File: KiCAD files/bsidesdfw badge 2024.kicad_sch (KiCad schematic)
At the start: 28 parts, among them Q1 BC548, U1 NE555P, U2 74HC595

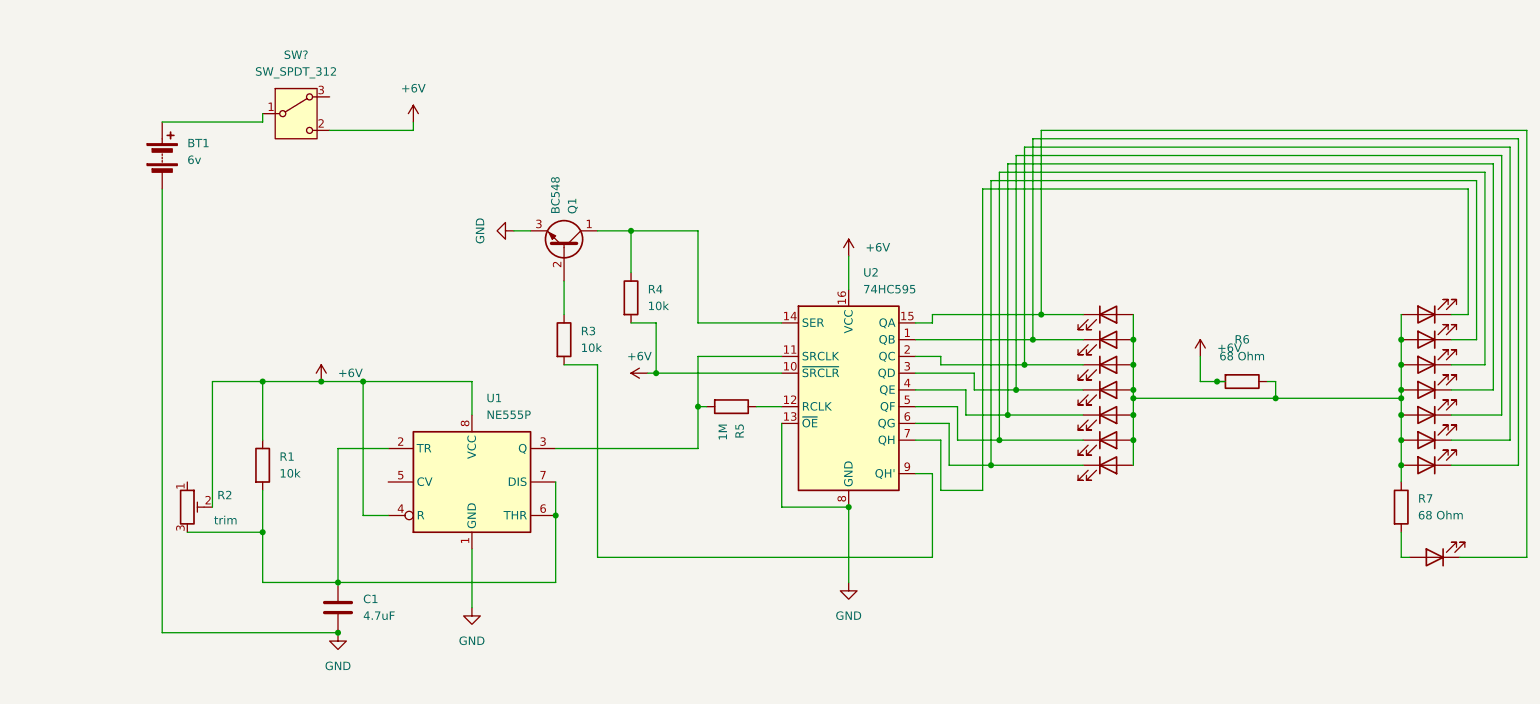
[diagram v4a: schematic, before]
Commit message: adjust the 555 drive
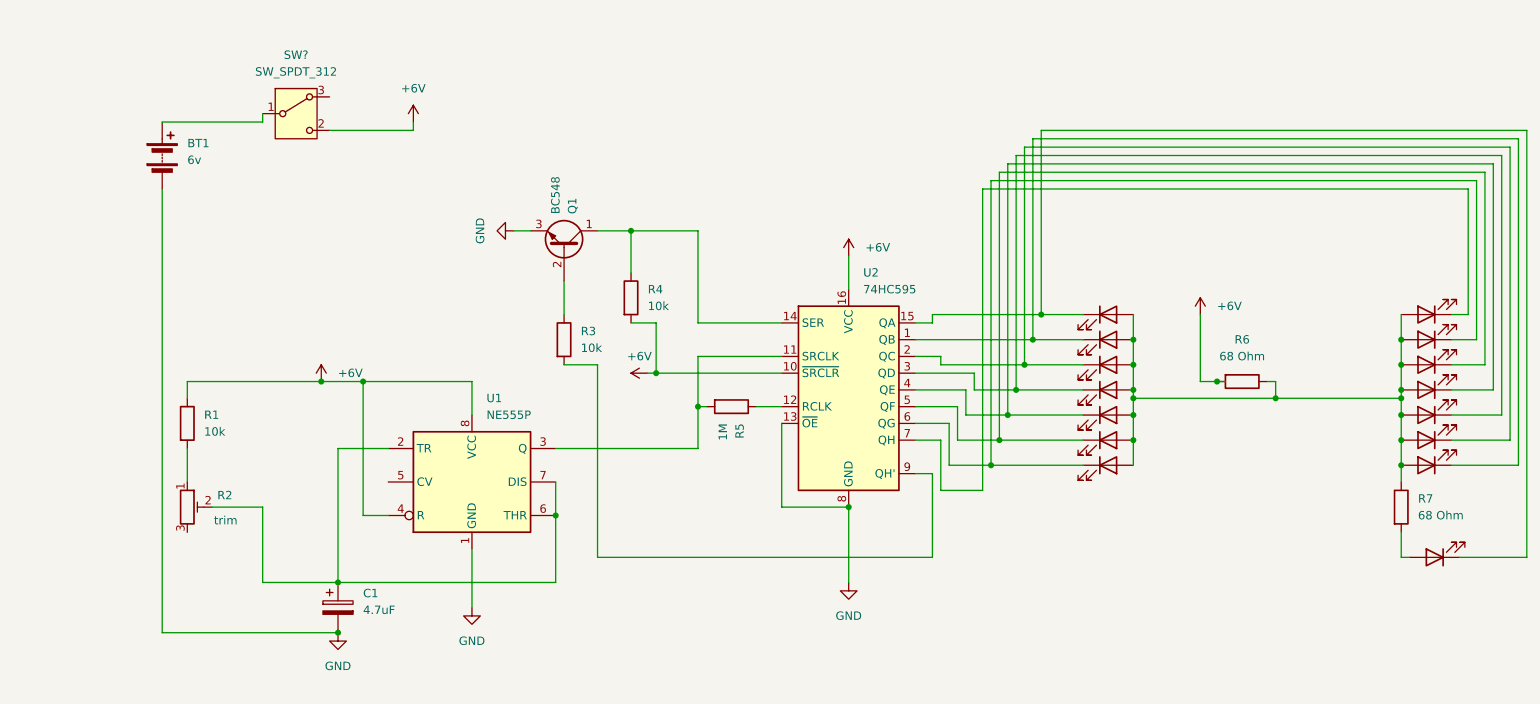
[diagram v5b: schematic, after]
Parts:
- removed C1: 4.7uF, symbol Device:C
- added C1: 4.7uF, symbol Device:C_Polarized
- renumbered D29 to D10, D28 to D11, D27 to D12, D26 to D13, D25 to D14, D32 to D15, D31 to D8, D30 to D9
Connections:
- net +6V: no longer R2.2
- net GND: now also C1.2
- net at U1.2 (TR), U1.6 (THR), U1.7 (DIS): now also R2.2, C1.1; no longer R1.2, R2.3
- net at R2.1: now also R1.2
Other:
- moved on the sheet: R1

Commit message: unsure if last changes saved, sending away
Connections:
- net at R1.2, R2.1: now also U1.7 (DIS)
- net at C1.1, R2.2, U1.2 (TR)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: no longer U1.7 (DIS)
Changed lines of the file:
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@@
+	)
+	(junction
+		(at 52.07 115.57)
+		(diameter 0)
+		(color 0 0 0 0)
 	)
 	(junction
@@
 	)
 	(junction
-		(at 107.95 124.46)
-		(diameter 0)
-		(color 0 0 0 0)
-	)
-	(junction
 		(at 129.54 107.95)
 		(diameter 0)
@@
 	(wire
 		(pts
+			(xy 43.18 115.57) (xy 52.07 115.57)
+		)
+		(stroke
+			(width 0)
+			(type default)
+		)
+	)
+	(wire
+		(pts
 			(xy 181.61 66.04) (xy 181.61 93.98)
 		)
@@
 	(wire
 		(pts
+			(xy 43.18 151.13) (xy 43.18 115.57)
+		)
+		(stroke
+			(width 0)
+			(type default)
+		)
+	)
+	(wire
+		(pts
 			(xy 243.84 109.22) (xy 251.46 109.22)
 		)
@@
 	(wire
 		(pts
-			(xy 52.07 114.3) (xy 52.07 119.38)
+			(xy 52.07 114.3) (xy 52.07 115.57)
 		)
 		(stroke
@@
 	(wire
 		(pts
+			(xy 111.76 119.38) (xy 111.76 151.13)
+		)
+		(stroke
+			(width 0)
+			(type default)
+		)
+	)
+	(wire
+		(pts
 			(xy 176.53 71.12) (xy 176.53 109.22)
 		)
@@
 	(wire
 		(pts
+			(xy 111.76 151.13) (xy 43.18 151.13)
+		)
+		(stroke
+			(width 0)
+			(type default)
+		)
+	)
+	(wire
+		(pts
 			(xy 152.4 85.09) (xy 152.4 90.17)
 		)
@@
 	(wire
 		(pts
+			(xy 107.95 119.38) (xy 111.76 119.38)
+		)
+		(stroke
+			(width 0)
+			(type default)
+		)
+	)
+	(wire
+		(pts
 			(xy 72.39 104.14) (xy 78.74 104.14)
 		)
@@
 	(wire
 		(pts
+			(xy 52.07 115.57) (xy 52.07 119.38)
+		)
+		(stroke
+			(width 0)
+			(type default)
+		)
+	)
+	(wire
+		(pts
 			(xy 173.99 116.84) (xy 187.96 116.84)
 		)
@@
 		)
 		(stroke
-			(width 0)
-			(type default)
-		)
-	)
-	(wire
-		(pts
-			(xy 107.95 119.38) (xy 107.95 124.46)
-		)
-		(stroke

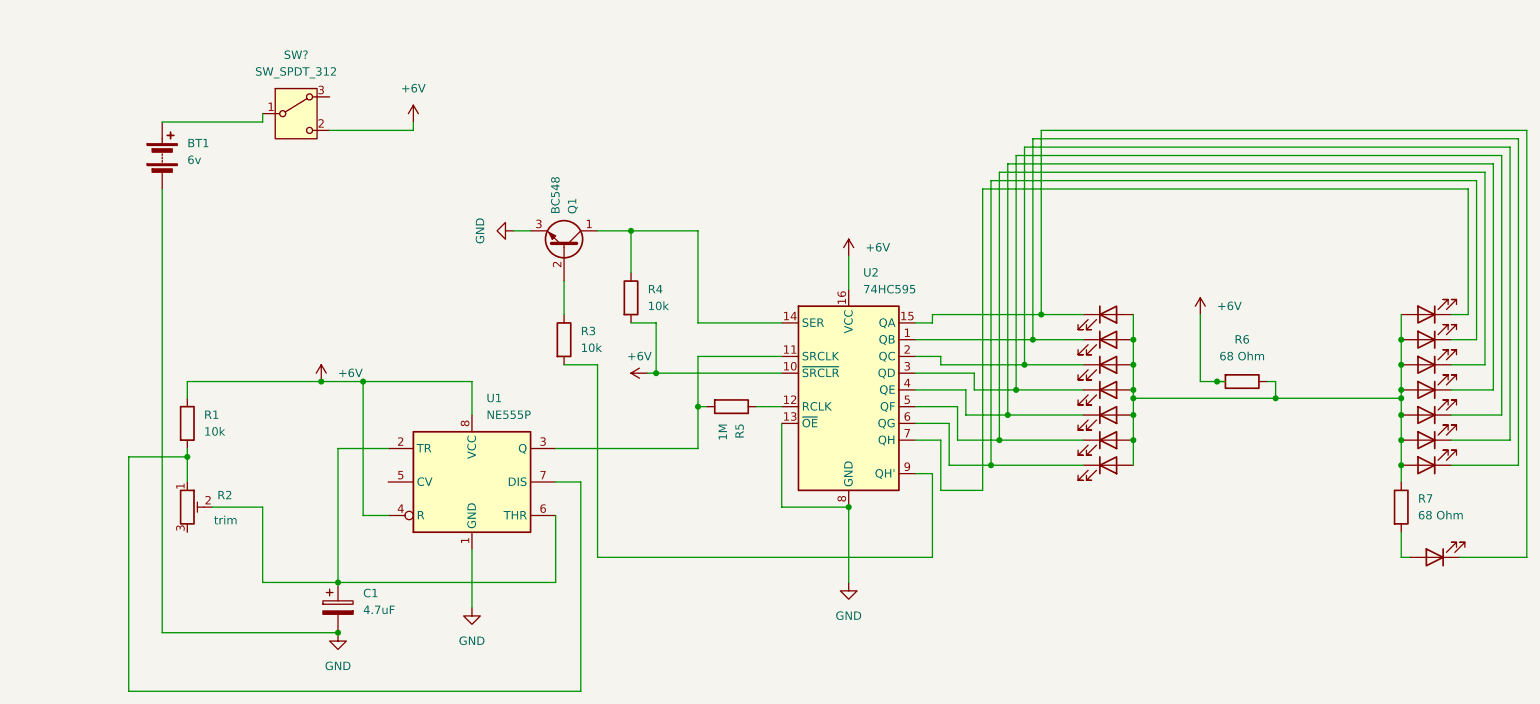
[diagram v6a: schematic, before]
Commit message: fixed broken footprint assignments; laid out components. Added a diode for reverse polarity protection.
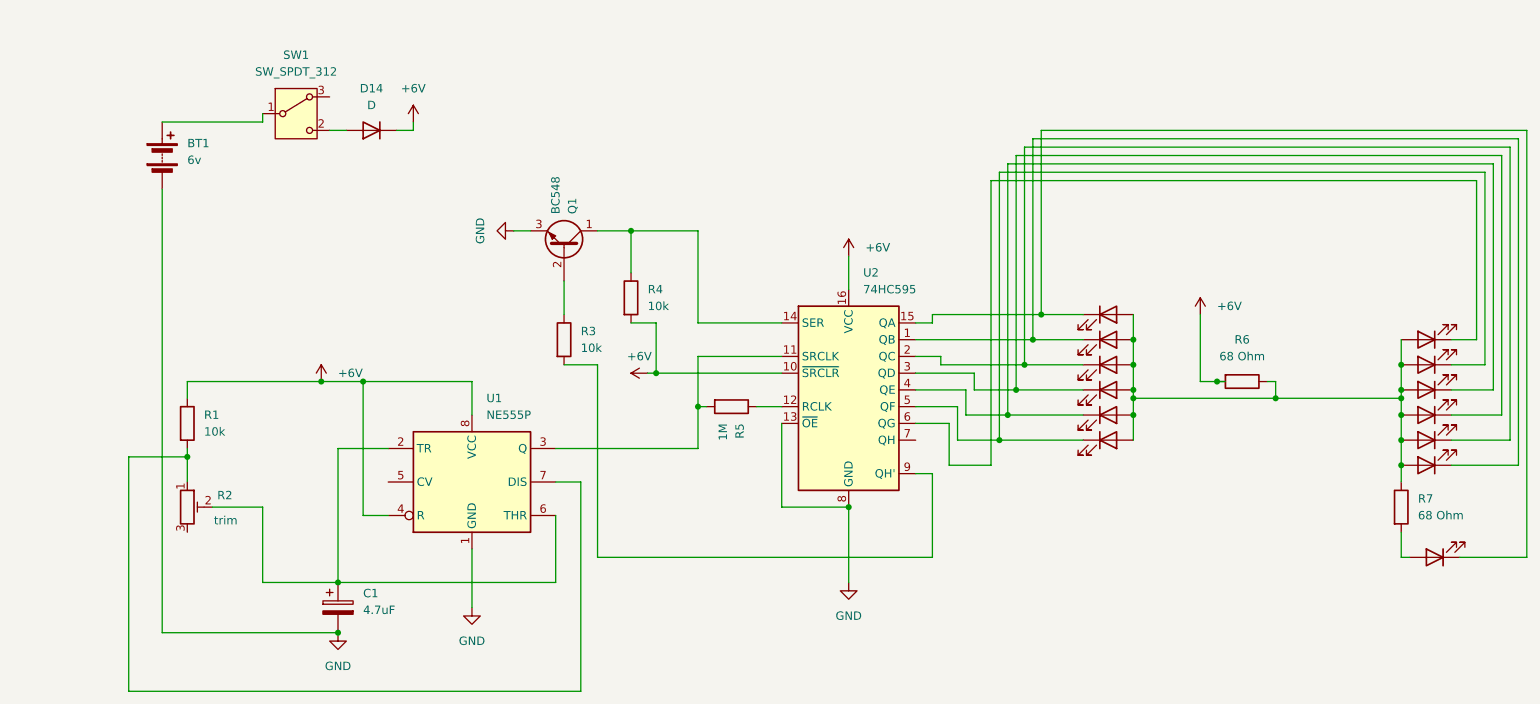
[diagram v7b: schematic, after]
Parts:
- removed D14, D7: ~, symbol Device:LED
- added D14: D, Diode_THT:D_T-1_P10.16mm_Horizontal, symbol Device:D
- BT1: footprint (none) -> SamacSys_Parts:1062
- C1: footprint (none) -> Capacitor_THT:CP_Radial_D4.0mm_P1.50mm
- D1, D2, D3, D4, D5, D6: footprint (none) -> LED_THT:LED_D5.0mm
- D10: renamed from D11; footprint (none) -> LED_THT:LED_D5.0mm
- D11: renamed from D12; footprint (none) -> LED_THT:LED_D5.0mm
- D12: renamed from D13; footprint (none) -> LED_THT:LED_D5.0mm
- D13: renamed from D15; footprint (none) -> LED_THT:LED_D5.0mm
- D7: renamed from D8; footprint (none) -> LED_THT:LED_D5.0mm
- D8: renamed from D9; footprint (none) -> LED_THT:LED_D5.0mm
- D9: renamed from D10; footprint (none) -> LED_THT:LED_D5.0mm
- R1, R3, R4, R5, R6, R7: footprint (none) -> Resistor_THT:R_Axial_DIN0309_L9.0mm_D3.2mm_P15.24mm_Horizontal
- R2: footprint (none) -> SamacSys_Parts:PT10RV10-103A0505-PM-S trim resistor
- SW1: renamed from SW?; footprint (none) -> SamacSys_Parts:SLW12745474ARAD
- U2: footprint (none) -> SamacSys_Parts:DIP794W53P254L1930H508Q16N
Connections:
- net +6V: now also D14.1 (K); no longer SW1.2 (C)
- new net: D14.2 (A), SW1.2 (C)

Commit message: placement finalized; tentative lanyard hole
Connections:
- net at BT1.1 (+): now also SW1.2 (C); no longer SW1.1 (B)
- net at D14.2 (A): now also SW1.1 (B); no longer SW1.2 (C)
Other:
- moved on the sheet: SW1
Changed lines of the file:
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@@
+	(wire
+		(pts
+			(xy 73.66 67.31) (xy 76.2 67.31)
+		)
+		(stroke
+			(width 0)
+			(type default)
+		)
+	)
 	(wire
 		(pts
@@
 	(wire
 		(pts
-			(xy 63.5 64.77) (xy 63.5 63.5)
-		)
-		(stroke
-			(width 0)
-			(type default)
-		)
-	)
-	(wire
-		(pts
 			(xy 236.22 130.81) (xy 237.49 130.81)
 		)
@@
 	(wire
 		(pts
-			(xy 73.66 66.04) (xy 76.2 66.04)
-		)
-		(stroke
-			(width 0)
-			(type default)
-		)
-	)
-	(wire
-		(pts
 			(xy 72.39 104.14) (xy 78.74 104.14)
 		)
@@
 		(pts
 			(xy 173.99 73.66) (xy 247.65 73.66)
+		)
+		(stroke
+			(width 0)
+			(type default)
+		)
+	)
+	(wire
+		(pts
+			(xy 76.2 67.31) (xy 76.2 66.04)
 		)
 		(stroke
@@
 	(symbol
 		(lib_id "Switch:SW_SPDT_312")
-		(at 68.58 63.5 0)
+		(at 68.58 67.31 180)
 		(unit 1)
 		(exclude_from_sim no)
@@
 		(fields_autoplaced yes)
 		(property "Reference" "SW1"
-			(at 68.58 54.61 0)
+			(at 68.58 58.42 0)
 			(effects
 				(font
@@
 		)
 		(property "Value" "SW_SPDT_312"
+			(at 68.58 60.96 0)
+			(effects
+				(font
+					(size 1.27 1.27)
+				)
+			)
+		)
+		(property "Footprint" "SamacSys_Parts:SLW12745474ARAD"
 			(at 68.58 57.15 0)
 			(effects
@@
 					(size 1.27 1.27)
 				)
-			)
-		)
-		(property "Footprint" "SamacSys_Parts:SLW12745474ARAD"
-			(at 68.58 73.66 0)
-			(effects
-				(font
-					(size 1.27 1.27)
-				)
 				(hide yes)
 			)
 		)
 		(property "Datasheet" "~"
-			(at 68.58 71.12 0)
+			(at 68.58 59.69 0)
 			(effects
 				(font
@@
 		)
 		(property "Description" "Switch, single pole double throw"
-			(at 68.58 63.5 0)
-			(effects
-				(font
+			(at 68.58 67.31 0)
+			(effects
+				(font
